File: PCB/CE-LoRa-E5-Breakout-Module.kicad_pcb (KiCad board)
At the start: 2 copper layers, 25.4 x 45.7 mm, 29 parts, among them J1 Conn_01x12_Male, J2 Conn_01x12_Male, SW1 BOOT, SW2 RESET, U1 LoRa-E5, U2 3V3 LDO - SOT23

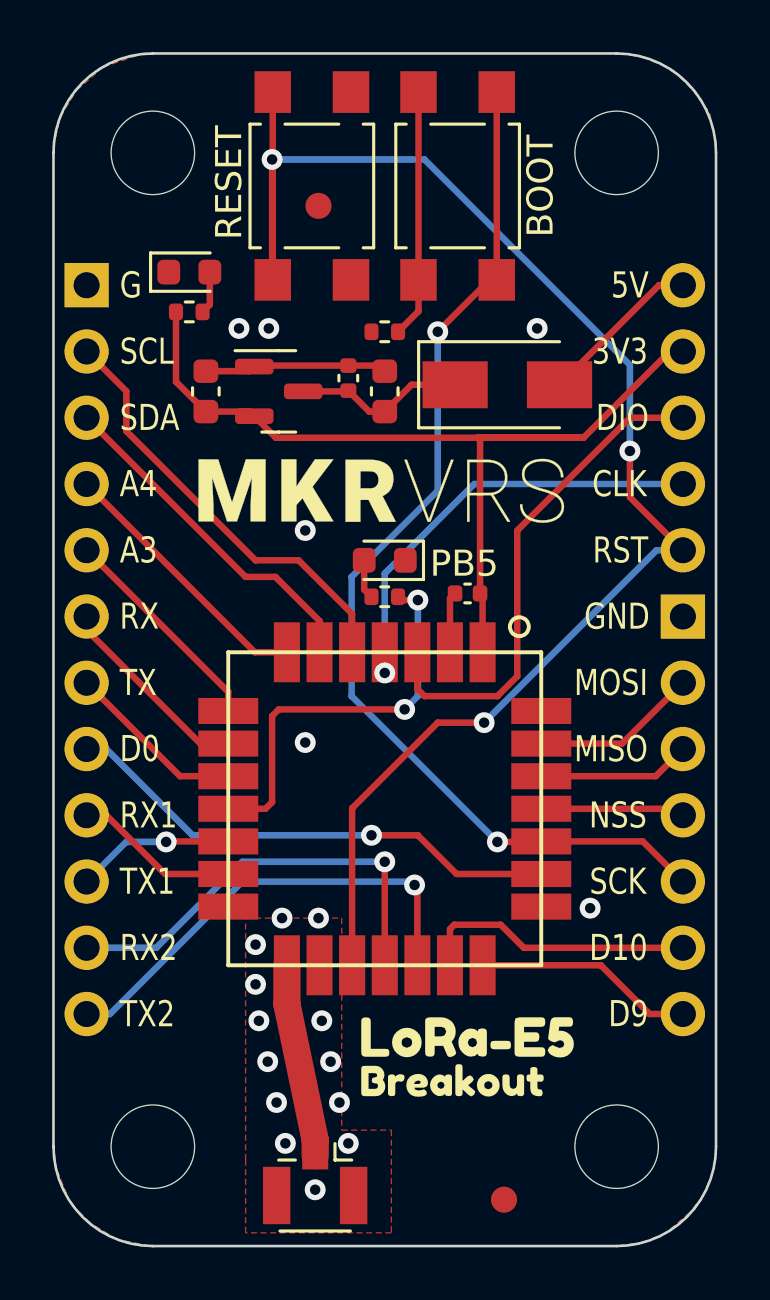
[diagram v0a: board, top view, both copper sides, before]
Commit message: v02 prototype with SMA connector option
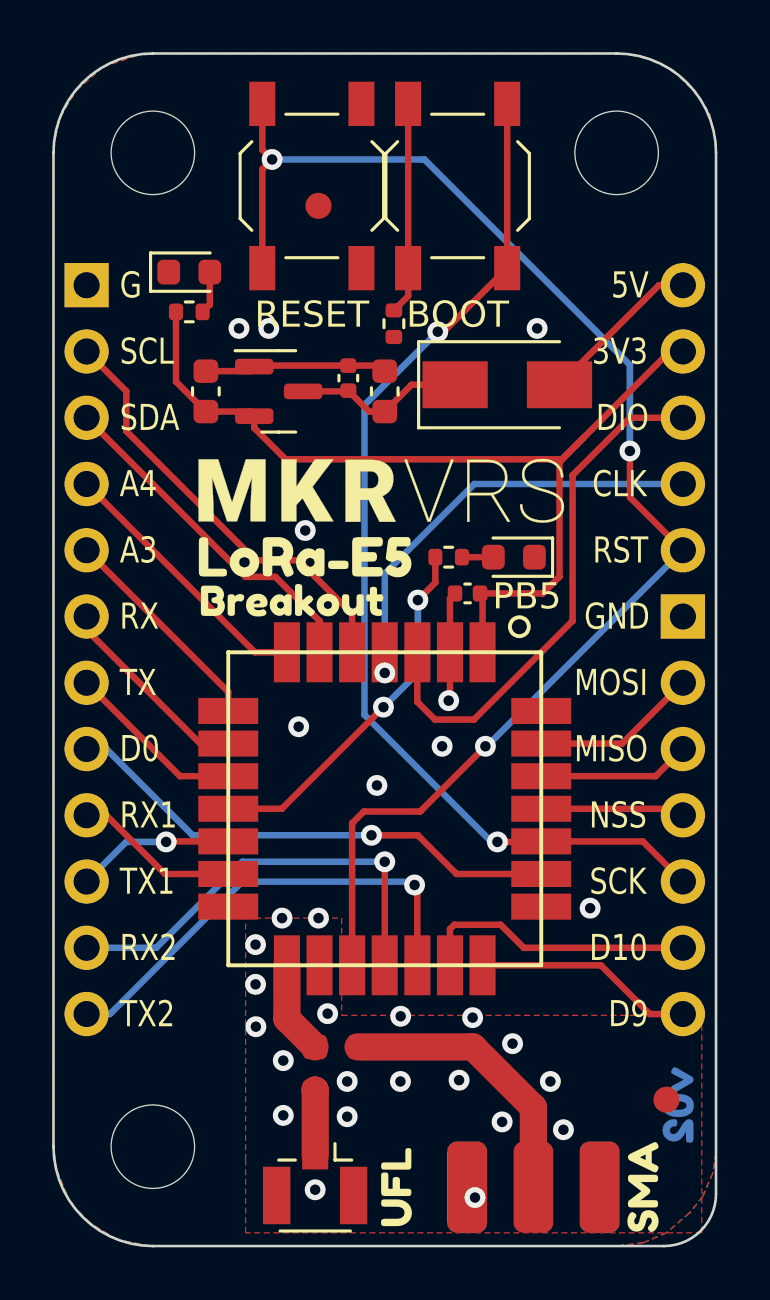
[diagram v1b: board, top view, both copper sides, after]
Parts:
- removed H2: MountingHole, MountingHole:MountingHole_3.2mm_M3
- added AE2: Antenna_Shield, CoreElectronics_Components:Conn_RF_SMA_EdgeMount, F.Cu at (134.0, 115.7)
- added SW3: SW_SPDT, CoreElectronics_Components:Jumper_Resistor_SPDT_0603_1608Metric, F.Cu at (125.6, 111.1)
- added kibuzzard-639FDA33: G***, kibuzzard-639FDA33, F.Cu at (138.2, 115.7)
- added kibuzzard-639FDA51: G***, kibuzzard-639FDA51, F.Cu at (128.7, 115.7)
- added kibuzzard-639FDCE0: G***, kibuzzard-639FDCE0, B.Cu at (139.5, 112.5)
- SW1, SW2: footprint Button_Switch_SMD:SW_SPST_TL3305A -> Button_Switch_SMD:SW_SPST_TL3342
- moved kibuzzard-635B4E81 19.4 mm to (125.2, 91.5)
- moved kibuzzard-635B4E71 19.4 mm to (124.7, 93.2)
- moved FID1 7.31 mm to (139.1, 112.3)
- moved D2 4.95 mm to (133.2, 91.5)
- moved R2 2.88 mm to (130.7, 91.5), turned to 180 degrees
- moved R3 0.47 mm to (128.6, 82.6), turned to -90 degrees
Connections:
- AE1 pad 1: /RF -> /RF_UFL
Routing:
- net /RF_SMA: track 0.00 -> 10.7 mm
- net /~{RST}: track 59.5 -> 54.0 mm
- net /RF: track 7.41 -> 3.57 mm
- net /RF_UFL: track 0.00 -> 2.53 mm
- net GND: track 9.37 -> 11.2 mm, vias 19 -> 29
- net Net-(R3-Pad1): track 9.51 -> 8.15 mm
- net /PB5/LED: track 15.5 -> 14.1 mm
- net /PA13/SWDIO: track 19.4 -> 20.4 mm
- net Net-(D2-Pad2): track 1.51 -> 0.70 mm
- net /PB13/BOOT/SCK: track 41.3 -> 40.7 mm
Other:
- outline, holes or cut-outs redrawn
- board text added: "Designed by Michael Ruppe at Core Electronics October 2022"
- board text removed: "Designed by Michael Ruppe at Core Electronics Octover 2022"

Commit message: v10
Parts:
- removed kibuzzard-639FDCE0: G***, kibuzzard-639FDCE0
- added G***: LOGO, datamatrix:CE09196, B.Cu at (125.4, 113.9)
- added kibuzzard-63AE194F: G***, kibuzzard-63AE194F, B.Cu at (139.0, 111.9)
- AE1: value Antenna_Shield -> UFL
- AE2: value Antenna_Shield -> SMA
- R4: renamed from SW3; value SW_SPDT -> 0R
- turned D2 to 0 degrees
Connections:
- D2 pad 1: GND -> Net-(D2-Pad1)
- D2 pad 2: Net-(D2-Pad2) -> +3V3
- R2 pad 1: Net-(D2-Pad2) -> Net-(D2-Pad1)
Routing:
- net Net-(D2-Pad1): track 0.00 -> 1.20 mm
- net +3V3: track 36.6 -> 37.6 mm
- net Net-(D2-Pad2): track 0.70 -> 0.00 mm
- net GND: vias 29 -> 28
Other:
- board text added: "PA0"
- board text added: "PA10"
- board text added: "PA13"
- board text added: "PA14"
- board text added: "PA15"
- board text added: "PA2"
- board text added: "PA3"
- board text added: "PA9"
- board text added: "PB10"
- board text added: "PB13"
- board text added: "PB14"
- board text added: "PB15"
- board text added: "PB3"
- board text added: "PB4"
- board text added: "PB6"
- board text added: "PB7"
- board text added: "PB9"
- board text added: "PC0"
- board text added: "PC1"
- board text added: "VIN"
- board text removed: "5V"
